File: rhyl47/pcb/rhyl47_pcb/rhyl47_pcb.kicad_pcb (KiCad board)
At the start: 2 copper layers, 228.8 x 76.2 mm, 124 parts, among them J2 USB_C_Receptacle_USB2.0_16P, SW1 SW_PUSH, SW10 SW_PUSH, SW11 SW_PUSH, SW12 SW_PUSH, SW13 SW_PUSH, SW14 SW_PUSH, SW15 SW_PUSH, SW16 SW_PUSH, SW17 SW_PUSH, SW18 SW_PUSH, SW19 SW_PUSH, SW2 SW_PUSH, SW20 SW_PUSH, SW21 SW_PUSH, SW22 SW_PUSH, SW23 SW_PUSH, SW24 SW_PUSH, SW25 SW_PUSH, SW26 SW_PUSH, SW27 SW_PUSH, SW28 SW_PUSH, SW29 SW_PUSH, SW3 SW_PUSH, SW30 SW_PUSH, SW31 SW_PUSH, SW32 SW_PUSH, SW33 SW_PUSH, SW34 SW_PUSH, SW35 SW_PUSH, SW36 SW_PUSH, SW37 SW_PUSH, SW38 SW_PUSH, SW39 SW_PUSH, SW4 SW_PUSH, SW40 SW_PUSH, SW41 SW_PUSH, SW42 SW_PUSH, SW43 SW_PUSH, SW44 SW_PUSH, SW45 SW_PUSH, SW46 SW_PUSH, SW47 SW_PUSH, SW48 boot, SW5 SW_PUSH, SW6 SW_PUSH, SW7 SW_PUSH, SW8 SW_PUSH, SW9 SW_PUSH, U1 RP2040, U2 W25Q16JVUXIQ, U4 XC6206P332MR, U5 SMF05CT1G, Y2 12MHz

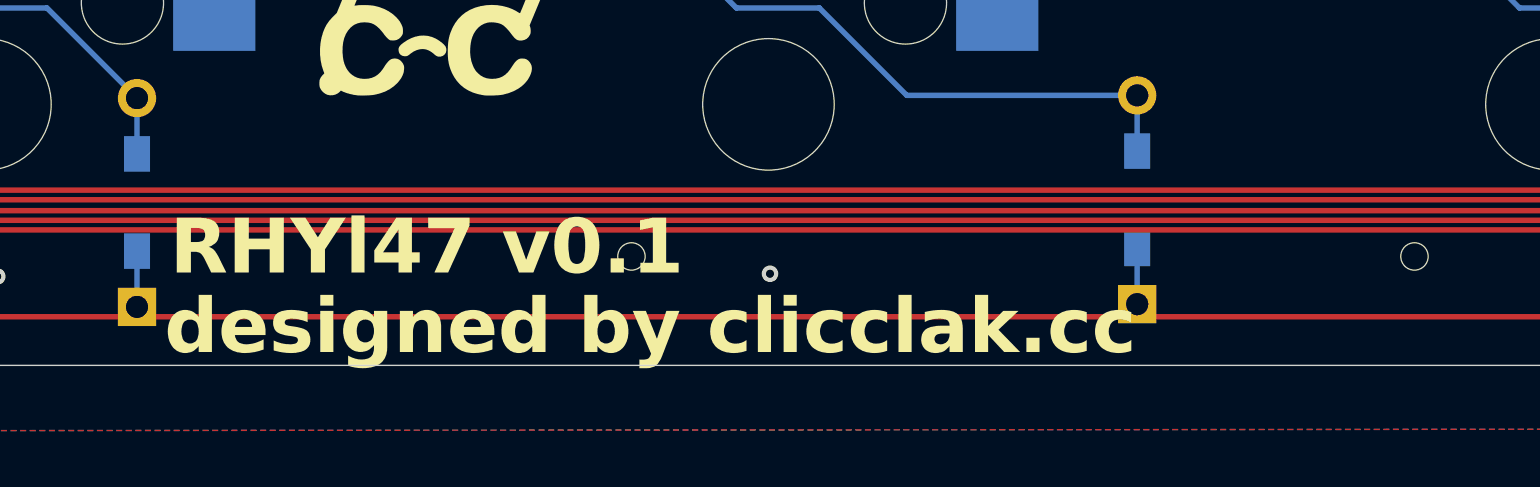
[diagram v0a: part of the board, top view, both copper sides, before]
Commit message: add rhyl47
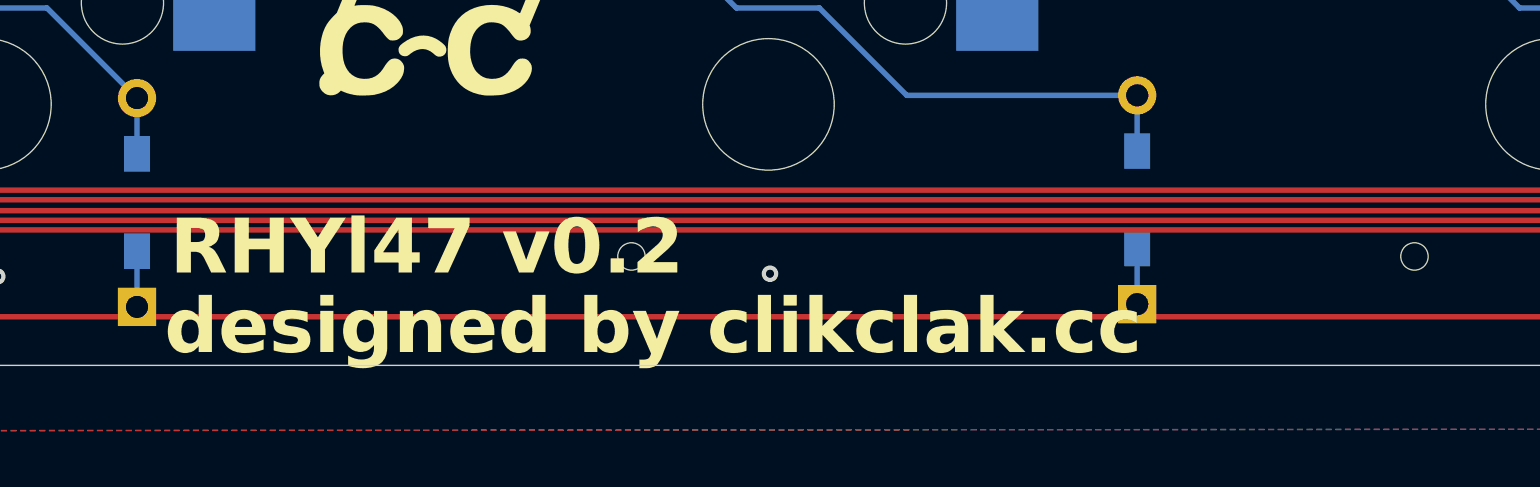
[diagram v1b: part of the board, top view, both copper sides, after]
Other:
- board text added: "RHYl47 v0.2"
- board text added: "designed by clikclak.cc"
- board text removed: "RHYl47 v0.1"
- board text removed: "designed by clicclak.cc"
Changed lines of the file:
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@@
 		(layer "Edge.Cuts")
 	)
-	(gr_text "RHYl47 v0.1"
+	(gr_text "RHYl47 v0.2"
 		(at 137.7 118.3 0)
 		(layer "F.SilkS")
@@
 			(justify left bottom)
 		)
-		(render_cache "RHYl47 v0.1" 0
+		(render_cache "RHYl47 v0.2" 0
 			(polygon
 				(pts
@@
 			(polygon
 				(pts
-					(xy 155.424459 117.96) (xy 156.491189 117.96) (xy 156.511462 117.956004) (xy 156.52666 117.943667)
-					(xy 156.542658 117.897047) (xy 156.545533 117.846915) (xy 156.541435 117.786083) (xy 156.52838 117.749126)
-					(xy 156.515126 117.736623) (xy 156.497627 117.73133) (xy 156.491189 117.731022) (xy 156.354505 117.732747)
-					(xy 156.094905 117.744822) (xy 156.107929 116.69892) (xy 156.108705 116.048189) (xy 156.093966 116.018334)
-					(xy 156.044925 115.993795) (xy 155.953611 115.982609) (xy 155.920679 115.986107) (xy 155.896675 115.994958)
-					(xy 155.872889 116.01143) (xy 155.673314 116.130486) (xy 155.415597 116.251248) (xy 155.277547 116.304644)
-					(xy 155.239891 116.323434) (xy 155.221319 116.350422) (xy 155.218928 116.369856) (xy 155.233608 116.450248)
-					(xy 155.251558 116.487887) (xy 155.275537 116.51664) (xy 155.297092 116.529545) (xy 155.321283 116.532687)
-					(xy 155.333112 116.530324) (xy 155.45124 116.489963) (xy 155.573914 116.437886) (xy 155.680253 116.383321)
-					(xy 155.787676 116.318125) (xy 155.837229 116.284249) (xy 155.871179 116.284249) (xy 155.86135 117.178734)
-					(xy 155.871179 117.744822) (xy 155.487621 117.731207) (xy 155.424459 117.731022) (xy 155.404819 117.735131)
-					(xy 155.390108 117.74826) (xy 155.375214 117.798557) (xy 155.372923 117.846915) (xy 155.376964 117.904844)
-					(xy 155.389614 117.941413) (xy 155.402789 117.954516) (xy 155.420132 117.959829)
+					(xy 155.304047 117.96) (xy 156.533199 117.96) (xy 156.552342 117.956001) (xy 156.56739 117.943641)
+					(xy 156.584505 117.895437) (xy 156.587543 117.846915) (xy 156.58366 117.790272) (xy 156.572111 117.753882)
+					(xy 156.5592 117.738795) (xy 156.542483 117.731794) (xy 156.533199 117.731022) (xy 156.033555 117.732762)
+					(xy 155.534734 117.744944) (xy 155.534734 117.720153) (xy 155.851698 117.462625) (xy 155.994559 117.337085)
+					(xy 156.124479 117.212832) (xy 156.226639 117.103993) (xy 156.316003 116.995211) (xy 156.379232 116.905111)
+					(xy 156.432125 116.8145) (xy 156.469431 116.734413) (xy 156.497733 116.653576) (xy 156.515294 116.578965)
+					(xy 156.524564 116.503461) (xy 156.525994 116.459982) (xy 156.522123 116.391649) (xy 156.510661 116.327982)
+					(xy 156.4925 116.270815) (xy 156.467612 116.218292) (xy 156.399531 116.128734) (xy 156.306617 116.058151)
+					(xy 156.187161 116.0073) (xy 156.038767 115.979075) (xy 155.945307 115.974794) (xy 155.847795 115.978644)
+					(xy 155.753706 115.989966) (xy 155.662574 116.008644) (xy 155.575862 116.034244) (xy 155.493938 116.066454)
+					(xy 155.417379 116.10489) (xy 155.346667 116.149183) (xy 155.329602 116.178221) (xy 155.332731 116.232933)
+					(xy 155.365571 116.309093) (xy 155.389508 116.338303) (xy 155.41532 116.354587) (xy 155.443387 116.351416)
+					(xy 155.514748 116.309536) (xy 155.591612 116.273568) (xy 155.672529 116.244438) (xy 155.757121 116.222624)
+					(xy 155.841099 116.209238) (xy 155.926889 116.203952) (xy 155.93688 116.203893) (xy 156.007173 116.207779)
+					(xy 156.070152 116.219346) (xy 156.121346 116.236661) (xy 156.165779 116.260262) (xy 156.200827 116.28779)
+					(xy 156.229561 116.32059) (xy 156.266439 116.398801) (xy 156.277355 116.485139) (xy 156.261947 116.603945)
+					(xy 156.213752 116.730525) (xy 156.124857 116.874936) (xy 155.979033 117.051727) (xy 155.743371 117.289068)
+					(xy 155.312595 117.681685) (xy 155.282852 117.715351) (xy 155.262665 117.753465) (xy 155.249703 117.835802)
+					(xy 155.253599 117.89531) (xy 155.265242 117.934654) (xy 155.278252 117.951326) (xy 155.295147 117.95918)
 				)
 			)
 		)
 	)
-	(gr_text "designed by clicclak.cc"
+	(gr_text "designed by clikclak.cc"
 		(at 137.5 121.2 0)
 		(layer "F.SilkS")
@@
 			(justify left bottom)
 		)
-		(render_cache "designed by clicclak.cc" 0
+		(render_cache "designed by clikclak.cc" 0
 			(polygon
 				(pts
@@
 			(polygon
 				(pts
-					(xy 164.412386 120.891263) (xy 164.6083 120.87675) (xy 164.808718 120.832889) (xy 164.96584 120.773415)
-					(xy 164.994119 120.75365) (xy 165.009796 120.731956) (xy 165.015422 120.702585) (xy 165.000739 120.629346)
-					(xy 164.98231 120.592696) (xy 164.957589 120.565467) (xy 164.936873 120.555291) (xy 164.913748 120.554998)
-					(xy 164.900628 120.559581) (xy 164.798083 120.601968) (xy 164.699741 120.633449) (xy 164.612352 120.65302)
-					(xy 164.525304 120.664377) (xy 164.440352 120.667903) (xy 164.362903 120.663841) (xy 164.293889 120.651041)
-					(xy 164.243404 120.63329) (xy 164.198658 120.608474) (xy 164.163039 120.579422) (xy 164.132155 120.54375)
-					(xy 164.084956 120.451969) (xy 164.055315 120.32128) (xy 164.046632 120.170013) (xy 164.050529 120.066137)
-					(xy 164.06217 119.972116) (xy 164.079634 119.894459) (xy 164.103522 119.825199) (xy 164.13131 119.768611)
-					(xy 164.164512 119.71928) (xy 164.200884 119.679302) (xy 164.242031 119.645877) (xy 164.336594 119.599404)
-					(xy 164.451936 119.578318) (xy 164.487979 119.577236) (xy 164.626577 119.591678) (xy 164.688358 119.608973)
-					(xy 164.739913 119.631689) (xy 164.761653 119.645258) (xy 164.792062 119.82209) (xy 164.799937 119.850601)
-					(xy 164.814226 119.867072) (xy 164.85471 119.875579) (xy 164.909666 119.871585) (xy 164.958344 119.859264)
-					(xy 164.988052 119.84346) (xy 165.007078 119.821985) (xy 165.012613 119.799131) (xy 164.99722 119.651377)
-					(xy 164.978419 119.577456) (xy 164.952448 119.517222) (xy 164.938974 119.497979) (xy 164.875119 119.444523)
-					(xy 164.767084 119.396637) (xy 164.615296 119.365371) (xy 164.50471 119.359371) (xy 164.416174 119.363267)
-					(xy 164.333328 119.374902) (xy 164.259795 119.393107) (xy 164.191547 119.418196) (xy 164.13073 119.448888)
-					(xy 164.074951 119.485877) (xy 163.979981 119.576991) (xy 163.904657 119.692998) (xy 163.849031 119.837303)
-					(xy 163.815217 120.014522) (xy 163.80642 120.181127) (xy 163.810309 120.296061) (xy 163.821901 120.399573)
-					(xy 163.839293 120.485119) (xy 163.863035 120.561586) (xy 163.890901 120.625132) (xy 163.924169 120.681233)
-					(xy 163.961147 120.728335) (xy 164.00298 120.769) (xy 164.100742 120.831762) (xy 164.222221 120.872555)
-					(xy 164.375338 120.890664)
-				)
-			)
+					(xy 164.871563 120.883447) (xy 164.962089 120.869517) (xy 165.010046 120.851583) (xy 165.044695 120.828732)
+					(xy 165.057431 120.803824) (xy 165.052822 120.779995) (xy 165.036186 120.749587) (xy 165.017498 120.722857)
+					(xy 164.840486 120.499924) (xy 164.725702 120.374325) (xy 164.601605 120.25087) (xy 164.418492 120.090879)
+					(xy 164.634519 119.886367) (xy 164.878418 119.618808) (xy 164.955826 119.525457) (xy 164.988845 119.477203)
+					(xy 164.998691 119.447177) (xy 164.984542 119.419425) (xy 164.934368 119.390321) (xy 164.839765 119.368504)
+					(xy 164.8127 119.367187) (xy 164.784981 119.371789) (xy 164.759875 119.388369) (xy 164.728314 119.425073)
+					(xy 164.598961 119.590296) (xy 164.458562 119.752178) (xy 164.34495 119.870544) (xy 164.220167 119.989274)
+					(xy 164.063573 120.010282) (xy 164.055181 120.011133) (xy 164.066294 118.856231) (xy 164.062252 118.834514)
+					(xy 164.049594 118.817909) (xy 164.002896 118.800286) (xy 163.947592 118.796636) (xy 163.888502 118.800632)
+					(xy 163.850175 118.812971) (xy 163.834799 118.826383) (xy 163.827206 118.844053) (xy 163.826081 118.856231)
+					(xy 163.827959 119.008829) (xy 163.834508 119.759441) (xy 163.834508 120.823241) (xy 163.838499 120.843381)
+					(xy 163.850807 120.859612) (xy 163.8983 120.879002) (xy 163.956018 120.883447) (xy 164.011448 120.879598)
+					(xy 164.048911 120.868286) (xy 164.066443 120.854996) (xy 164.075578 120.837794) (xy 164.077407 120.823241)
+					(xy 164.074995 120.629037) (xy 164.058112 120.234616) (xy 164.2209 120.212756) (xy 164.454762 120.426268)
+					(xy 164.664973 120.65891) (xy 164.787055 120.819944) (xy 164.814928 120.859087) (xy 164.842893 120.87871)
+				)
+			)
